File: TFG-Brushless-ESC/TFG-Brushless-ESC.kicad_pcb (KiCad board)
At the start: 4 copper layers, 100 x 51 mm, 140 parts, among them J1 MOTOR, J2 USB C Receptacle, J3 HALL SENSORS, J4 SWD-I2C, J5 24V IN, Q1 TK58E06N1, Q2 TK58E06N1, Q3 TK58E06N1, Q4 TK58E06N1, Q5 TK58E06N1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

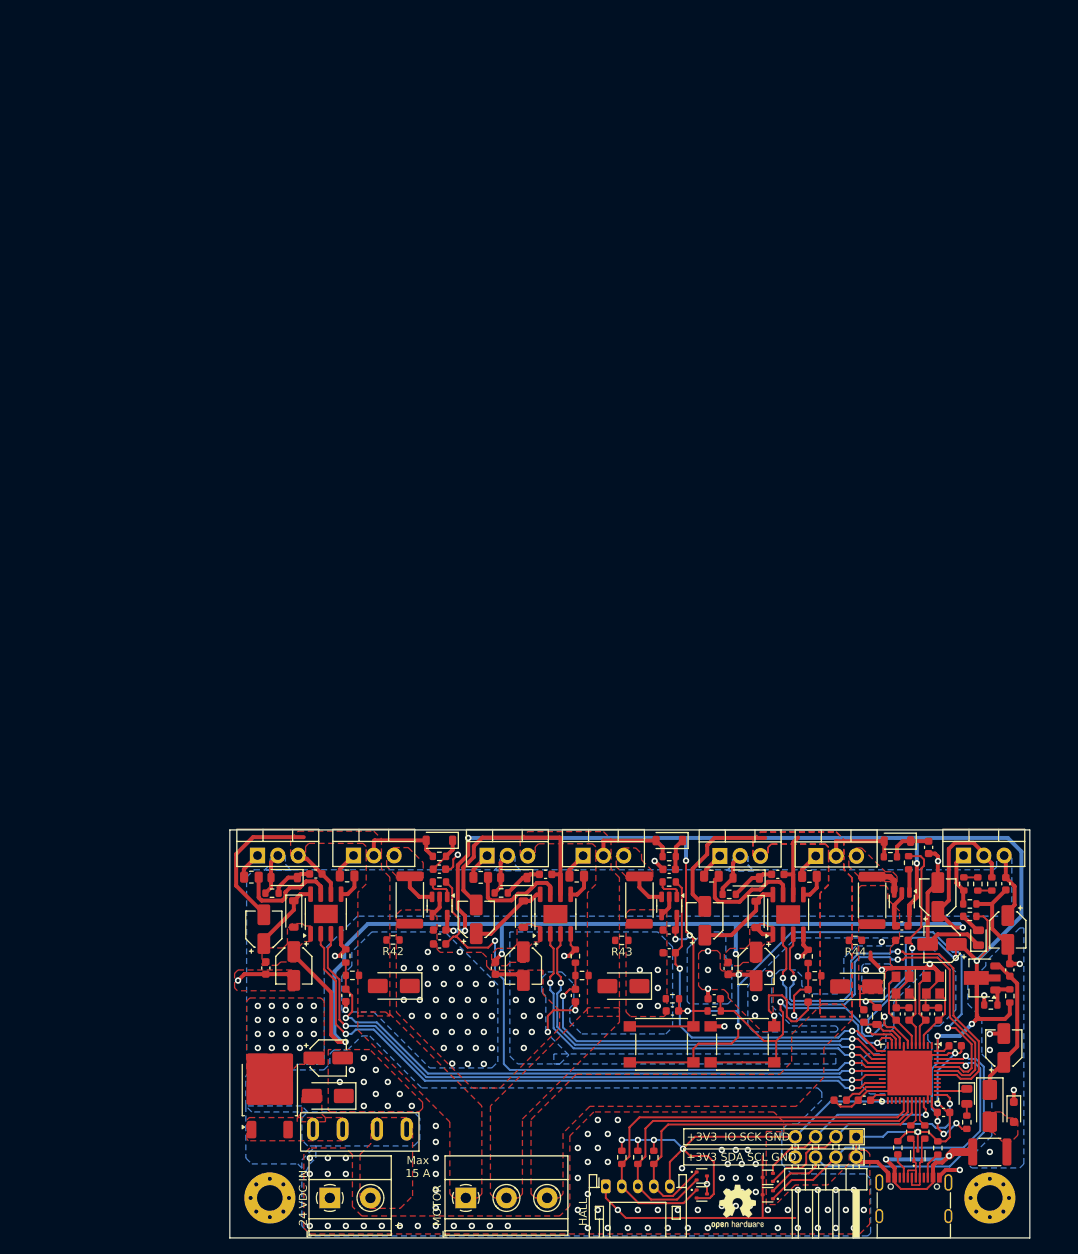
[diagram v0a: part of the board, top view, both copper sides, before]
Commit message: Change motor terminal blocks and new half bridge layaout
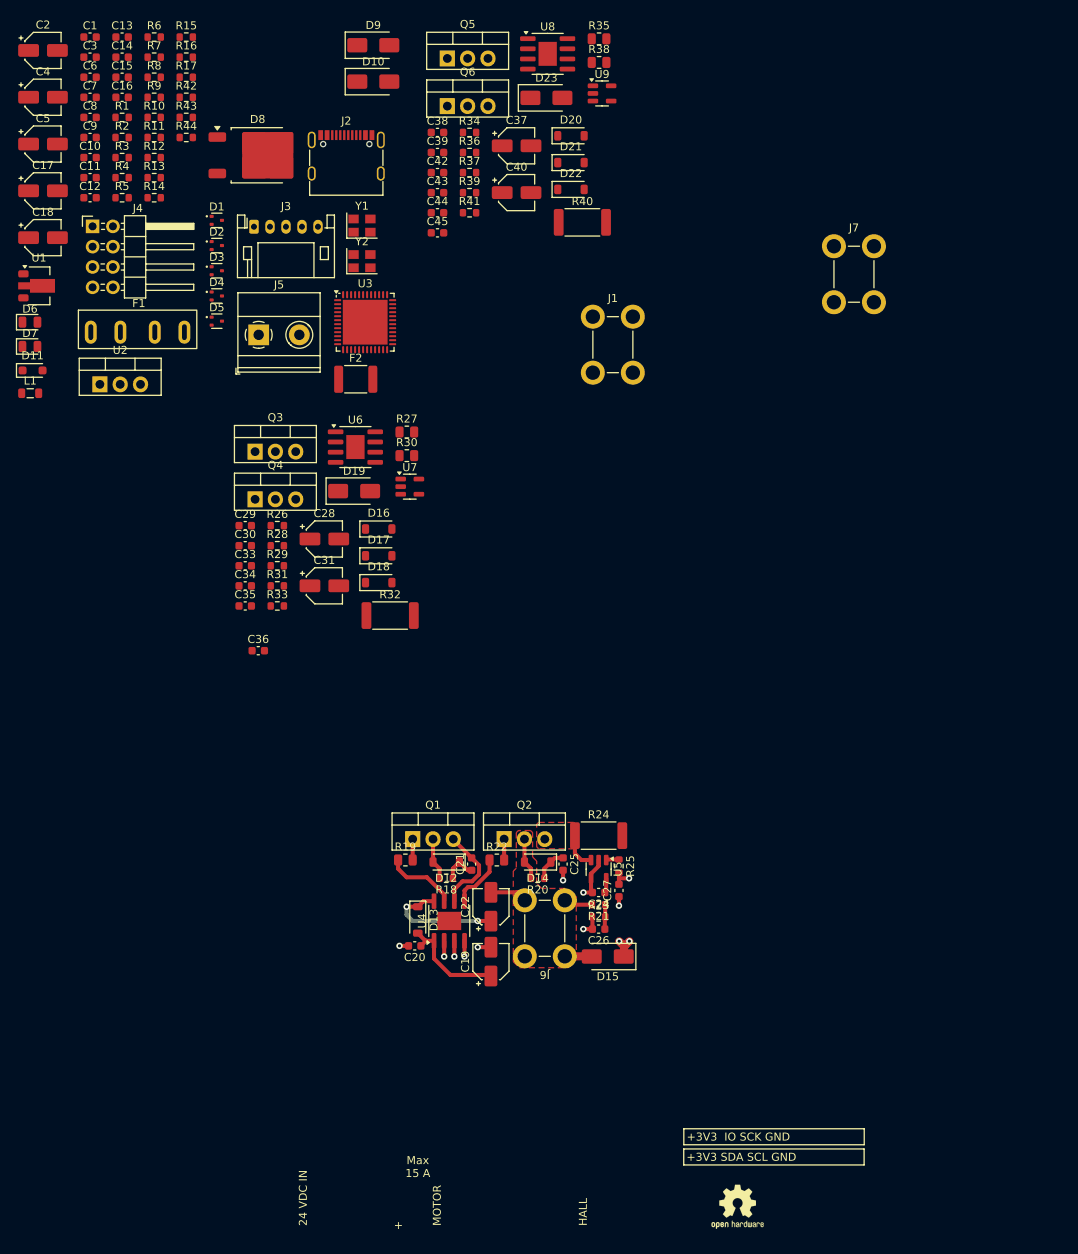
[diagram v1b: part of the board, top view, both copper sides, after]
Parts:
- removed the REF** at (139.3, 161.5)
- removed the REF** at (49.3, 161.5)
- removed the REF** at (116.8, 162.5)
- removed SW1: BOOT0, Button_Switch_SMD:SW_Push_1P1T_NO_6x6mm_H9.5mm
- removed SW2: NRST, Button_Switch_SMD:SW_Push_1P1T_NO_6x6mm_H9.5mm
- added J6: U, TFG-Brushless-ESC:Screw_Terminal, F.Cu at (83.6, 127.9)
- added J7: W, TFG-Brushless-ESC:Screw_Terminal, F.Cu at (122.3, 46.0)
- F1: value 15A -> 20A
- J1: value MOTOR -> V; footprint TerminalBlock_Phoenix:TerminalBlock_Phoenix_MKDS-1,5-3-5.08_1x03_P5.08mm_Horizontal -> TFG-Brushless-ESC:Screw_Terminal
- moved C7 165.8 mm to (26.8, 23.9)
- moved C1 163.8 mm to (26.8, 16.4), turned to 0 degrees
- moved R17 163.0 mm to (38.8, 21.4), turned to 0 degrees
- moved R10 161.8 mm to (34.8, 26.5), turned to 0 degrees
- moved R9 160.9 mm to (34.8, 23.9), turned to 0 degrees
- moved R6 159.9 mm to (34.8, 16.4), turned to 0 degrees
- moved C4 159.3 mm to (20.9, 23.9), turned to 0 degrees
- moved C2 158.5 mm to (20.9, 18.1), turned to 0 degrees
- moved C14 157.2 mm to (30.8, 18.9), turned to 0 degrees
- moved C18 157.1 mm to (20.9, 41.5), turned to 0 degrees
- moved C9 156.8 mm to (26.8, 29.0)
- moved C8 156.4 mm to (26.8, 26.5), turned to 0 degrees
- moved R11 156.2 mm to (34.8, 29.0), turned to 0 degrees
- moved R1 156.1 mm to (30.8, 26.5), turned to 0 degrees
- moved C13 155.8 mm to (30.8, 16.4), turned to 0 degrees
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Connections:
- J1 pad 1: /U -> /V
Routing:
- net +3V3: track 303.3 -> 1.86 mm, vias 20 -> 0
- net GND: track 242.3 -> 19.8 mm, vias 171 -> 9
- net +12V: track 142.0 -> 13.5 mm, vias 4 -> 0
- net /BOOT0: track 86.4 -> 0.00 mm, vias 3 -> 0
- net /PB10: track 84.4 -> 1.97 mm, vias 2 -> 1
- net /PB1: track 82.7 -> 1.97 mm, vias 2 -> 1
- net /PA7: track 79.2 -> 2.79 mm, vias 2 -> 1
- net /PB0: track 77.7 -> 3.07 mm, vias 2 -> 0
- net /PA6: track 55.2 -> 0.00 mm, vias 2 -> 0
- net /PA8: track 55.1 -> 0.00 mm
- net /PB6: track 54.9 -> 0.00 mm, vias 2 -> 0
- net /PA5: track 54.4 -> 0.00 mm, vias 2 -> 0
- net /PB7: track 54.1 -> 0.00 mm, vias 2 -> 0
- net /PA9: track 51.8 -> 0.00 mm
- net /PA4: track 50.7 -> 0.00 mm, vias 2 -> 0
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- removed copper zone on F.Cu, net +12V
- removed copper zone on B.Cu, net +24V
- removed copper zone on F.Cu, net +24V
- removed copper zone on F.Cu, net /24V fused
- removed copper zone on F.Cu, net /24V in
- removed copper zone on F.Cu, net /5V fused
- removed copper zone on F.Cu, net /Half-Bridge-V/Shunt
- removed copper zone on F.Cu, net /Half-Bridge-W/Shunt
- removed copper zone on F.Cu, net /V
- removed copper zone on F.Cu, net /W
- removed copper zone on B.Cu, net GND
- removed copper zone on F.Cu, net GND
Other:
- board outline removed
- board text removed: "Designed by humans on Earth"
- board text removed: "Dimensions: 100 x 51 mm Distance between screw holes: 90 mm"
- board text removed: "Mira a la pizarra"
- board text removed: "github.com/AdriTeixeHax"

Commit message: PCB v2
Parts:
- added D24: DESD5V0U1BA, Diode_SMD:D_SOD-323_HandSoldering, F.Cu at (108.6, 154.4)
- added D25: DESD5V0U1BA, Diode_SMD:D_SOD-323_HandSoldering, F.Cu at (72.5, 150.2)
- added R45: 10k, Resistor_SMD:R_0603_1608Metric, F.Cu at (150.7, 157.3)
- added R46: 10k, Resistor_SMD:R_0603_1608Metric, F.Cu at (150.7, 161.3)
- added REF**: MountingHole_3.2mm_M3_Pad_Via, MountingHole:MountingHole_3.2mm_M3_Pad_Via, F.Cu at (69.8, 141.1)
- added REF**: MountingHole_3.2mm_M3_Pad_Via, MountingHole:MountingHole_3.2mm_M3_Pad_Via, F.Cu at (154.9, 141.1)
- added SW1: BOOT0, Button_Switch_SMD:SW_Push_1P1T_NO_6x6mm_H9.5mm, F.Cu at (145.3, 142.1)
- added SW2: NRST, Button_Switch_SMD:SW_Push_1P1T_NO_6x6mm_H9.5mm, F.Cu at (135.0, 142.1)
- F1: value 20A -> 15A
- J2: footprint Connector_USB:USB_C_Receptacle_G-Switch_GT-USB-7010ASV -> Connector_USB:USB_C_Receptacle_XKB_U262-16XN-4BVC11
- moved C6 168.5 mm to (148.5, 138.0)
- moved C2 166.6 mm to (114.8, 155.7), turned to 180 degrees
- moved R6 165.6 mm to (125.0, 155.2), turned to 180 degrees
- moved C1 163.2 mm to (109.7, 157.0), turned to 180 degrees
- moved J4 162.8 mm to (147.1, 150.1), turned to -90 degrees
- moved R10 161.6 mm to (135.8, 152.6), turned to 180 degrees
- moved C14 160.0 mm to (124.7, 148.4)
- moved R9 159.0 mm to (128.2, 152.6)
- moved R1 158.3 mm to (125.0, 153.7)
- moved R2 158.2 mm to (145.5, 138.0), turned to 180 degrees
- moved D1 158.2 mm to (150.3, 155.2)
- moved C13 157.7 mm to (124.7, 143.1)
- moved C7 157.5 mm to (121.6, 149.8)
- moved C15 156.7 mm to (124.7, 146.9)
- moved R15 153.9 mm to (91.5, 161.1), turned to 180 degrees
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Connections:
- D3 pad 1: /PA10 -> /PA8
- D4 pad 1: /PA8 -> /PA10
- R13 pad 1: /PA10 -> /PA8
- R15 pad 1: /PA8 -> /PA10
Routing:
- net +3V3: track 1.86 -> 281.3 mm, vias 0 -> 10
- net GND: track 19.8 -> 206.2 mm, vias 9 -> 69
- net +12V: track 13.5 -> 134.4 mm
- net /BOOT0: track 0.00 -> 63.5 mm, vias 0 -> 2
- net /PA7: track 2.79 -> 62.6 mm, vias 1 -> 2
- net /PA0: track 0.00 -> 59.6 mm, vias 0 -> 2
- net /PB1: track 1.97 -> 59.9 mm, vias 1 -> 2
- net +24V: track 5.24 -> 62.9 mm, vias 0 -> 16
- net /PB10: track 1.97 -> 59.0 mm, vias 1 -> 2
- net /SWDIO: track 0.00 -> 55.8 mm, vias 0 -> 1
- net /PB0: track 3.07 -> 58.2 mm, vias 0 -> 2
- net /PA1: track 0.00 -> 54.5 mm, vias 0 -> 2
- net /SWSCK: track 0.00 -> 48.3 mm, vias 0 -> 1
- net /I2C_SDA: track 0.00 -> 46.4 mm
- net /USB_R_N: track 0.00 -> 46.1 mm, vias 0 -> 2
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- added copper zone on F.Cu, net +12V
- added copper zone on B.Cu, net +24V
- added copper zone on F.Cu, net +24V
- added copper zone on F.Cu, net /24V fused
- added copper zone on F.Cu, net /24V in
- added copper zone on F.Cu, net /Half-Bridge-V/Shunt
- added copper zone on F.Cu, net /Half-Bridge-W/Shunt
- added copper zone on F.Cu, net /V
- added copper zone on F.Cu, net /W
- added copper zone on F.Cu, net GND
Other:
- board outline added: 95.4 x 49.3 mm
- board text added: "3V3 IO SCK GND"
- board text added: "3V3 SDA SCL GND"
- board text removed: "+3V3 IO SCK GND"
- board text removed: "+3V3 SDA SCL GND"

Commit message: PCB v3
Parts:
- removed the REF** at (69.8, 141.1)
- removed the REF** at (154.9, 141.1)
- added ?: , , F.Cu at (104.3, 59.3)
- added REF**: MountingHole_2.2mm_M2_Pad_Via, MountingHole:MountingHole_2.2mm_M2_Pad_Via, F.Cu at (104.3, 94.7)
- added REF**: MountingHole_2.2mm_M2_Pad_Via, MountingHole:MountingHole_2.2mm_M2_Pad_Via, F.Cu at (204.3, 57.7)
- added REF**: MountingHole_2.2mm_M2_Pad_Via, MountingHole:MountingHole_2.2mm_M2_Pad_Via, F.Cu at (104.3, 57.7)
- added REF**: MountingHole_2.2mm_M2_Pad_Via, MountingHole:MountingHole_2.2mm_M2_Pad_Via, F.Cu at (204.3, 94.7)
- D8: value FERD30H100SB -> STPS30100ST; footprint Package_TO_SOT_SMD:TO-252-2 -> Package_TO_SOT_THT:TO-220-3_Vertical
- moved SW1 94.3 mm to (203.7, 68.0), turned to -90 degrees
- moved SW2 93.7 mm to (203.7, 78.3), turned to -90 degrees
- moved R13 93.7 mm to (156.4, 90.5), turned to -90 degrees
- moved R14 92.6 mm to (156.4, 93.5), turned to -90 degrees
- moved R15 91.5 mm to (156.4, 96.6), turned to -90 degrees
- moved R46 91.2 mm to (203.5, 86.9)
- moved D3 90.9 mm to (162.8, 88.7)
- moved D4 90.9 mm to (166.8, 88.7)
- moved J3 90.9 mm to (159.8, 91.9)
- moved REF** 89.4 mm to (119.0, 77.0)
- moved C6 89.3 mm to (199.6, 64.8), turned to 90 degrees
- moved C8 89.1 mm to (182.2, 93.5)
- moved R2 88.6 mm to (199.6, 67.8), turned to -90 degrees
- moved D7 88.5 mm to (175.8, 94.4)
- moved R17 88.5 mm to (172.5, 94.4)
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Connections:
- net Net-(D13-K) renamed /Half-Bridge-U/VB
- net Net-(D17-K) renamed /Half-Bridge-V/VB
- net Net-(D21-K) renamed /Half-Bridge-W/VB
- C26 pad 1: /PB0 -> /PB1
- C27 pad 2: /PA7 -> /PB0
- C35 pad 1: /PA4 -> /PA5
- C36 pad 2: /PA3 -> /PA4
- D3 pad 1: /PA8 -> /PB3
- D3 pad 2: /PA9 -> /PB4
- D4 pad 1: /PA10 -> /PB5
- J3 pad 2: /PA8 -> /PB3
- J3 pad 3: /PA9 -> /PB4
- J3 pad 4: /PA10 -> /PB5
- J5 pad 1: GND -> /24V in
- J5 pad 2: /24V in -> GND
- R13 pad 1: /PA8 -> /PB3
- R14 pad 1: /PA9 -> /PB4
- R15 pad 1: /PA10 -> /PB5
- R21 pad 1: /PB0 -> /PB1
- R23 pad 2: /PB0 -> /PB1
- R25 pad 2: /PA7 -> /PB0
- R29 pad 1: /PA4 -> /PA5
- R31 pad 2: /PA4 -> /PA5
- R33 pad 2: /PA3 -> /PA4
- U4 pad 2: /PB10 -> /PA9
- U4 pad 3: /PB1 -> /PA8
- U6 pad 2: /PA6 -> /PA7
- U6 pad 3: /PA5 -> /PA6
- U8 pad 2: /PB7 -> /PA3
- U8 pad 3: /PB6 -> /PA2
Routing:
- net /PB10: track 59.0 -> 0.00 mm, vias 2 -> 0
- net /PB5: track 0.00 -> 44.1 mm
- net /PB4: track 0.00 -> 43.5 mm
- net /PB3: track 0.00 -> 42.8 mm
- net /PA10: track 37.2 -> 0.00 mm
- net /PB6: track 37.0 -> 0.00 mm, vias 2 -> 0
- net /PB7: track 34.7 -> 0.00 mm, vias 2 -> 0
- net /PA8: track 33.9 -> 65.0 mm
- net /PA9: track 35.4 -> 65.8 mm
- net /USB_R_N: track 46.1 -> 15.9 mm, vias 2 -> 0
- net /USB_R_P: track 45.5 -> 16.0 mm, vias 2 -> 0
- net /PA1: track 54.5 -> 30.1 mm, vias 2 -> 0
- net /PA7: track 62.6 -> 39.8 mm, vias 2 -> 0
- net /PA0: track 59.6 -> 38.7 mm, vias 2 -> 0
- net /SWSCK: track 48.3 -> 32.4 mm, vias 1 -> 2
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- added copper zone on In1.Cu, net /24V fused
- added copper zone on In2.Cu, net /24V fused
- added copper zone on B.Cu, net /24V in
- added copper zone on In1.Cu, net /24V in
- added copper zone on In2.Cu, net /24V in
- added copper zone on B.Cu, net /U
- added copper zone on In1.Cu, net /U
- added copper zone on In2.Cu, net /U
- added copper zone on B.Cu, net /V
- added copper zone on In1.Cu, net /V
- added copper zone on In2.Cu, net /V
- added copper zone on B.Cu, net /W
- added copper zone on In1.Cu, net /W
- added copper zone on In2.Cu, net /W
- added copper zone on B.Cu, net GND
- removed copper zone on F.Cu, net +12V
- removed copper zone on F.Cu, net +24V
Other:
- board size 95.4 x 49.3 mm -> 107 x 44 mm
- board text added: "24Vcc IN"
- board text added: "By AdriTeixeHax"
- board text added: "Hall"
- board text added: "RTSpeed"
- board text added: "USB Type C"
- board text added: "V IO CLK G V SCK SCL G"
- board text added: "_____________"
- board text added: "github.com/AdriTeixeHax"
- board text removed: "+"
- board text removed: "24 VDC IN"
- board text removed: "24V In"
- board text removed: "3V3 IO SCK GND"
- board text removed: "3V3 SDA SCL GND"
- board text removed: "HALL"
- board text removed: "MOTOR"
- board text removed: "Max 15 A"
- board text removed: "OUT"
- board text removed: "Reg 12V"
- board text removed: "Reg 5V"
- board text removed: "U"
- board text removed: "USB C"
- board text removed: "V"
- board text removed: "W"
- board text removed: "uC"

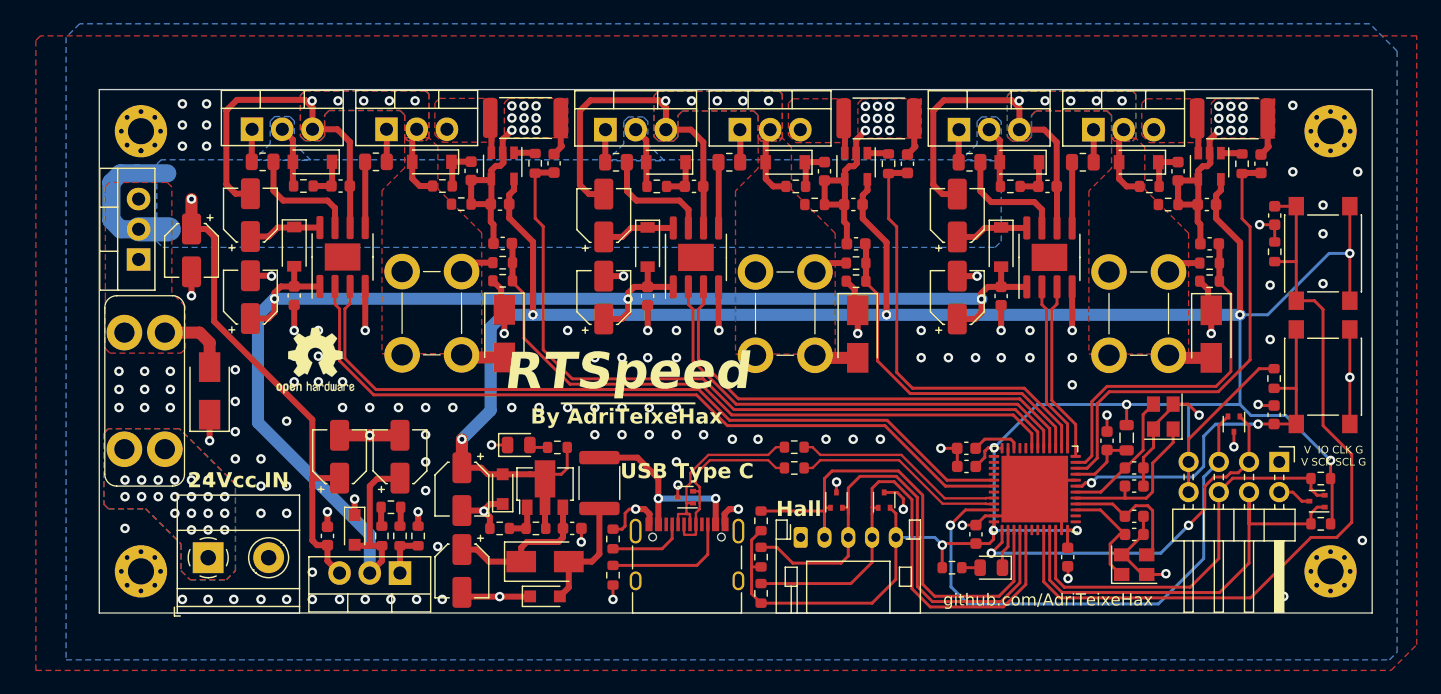
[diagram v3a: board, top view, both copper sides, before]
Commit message: updated main power connector to phoenix
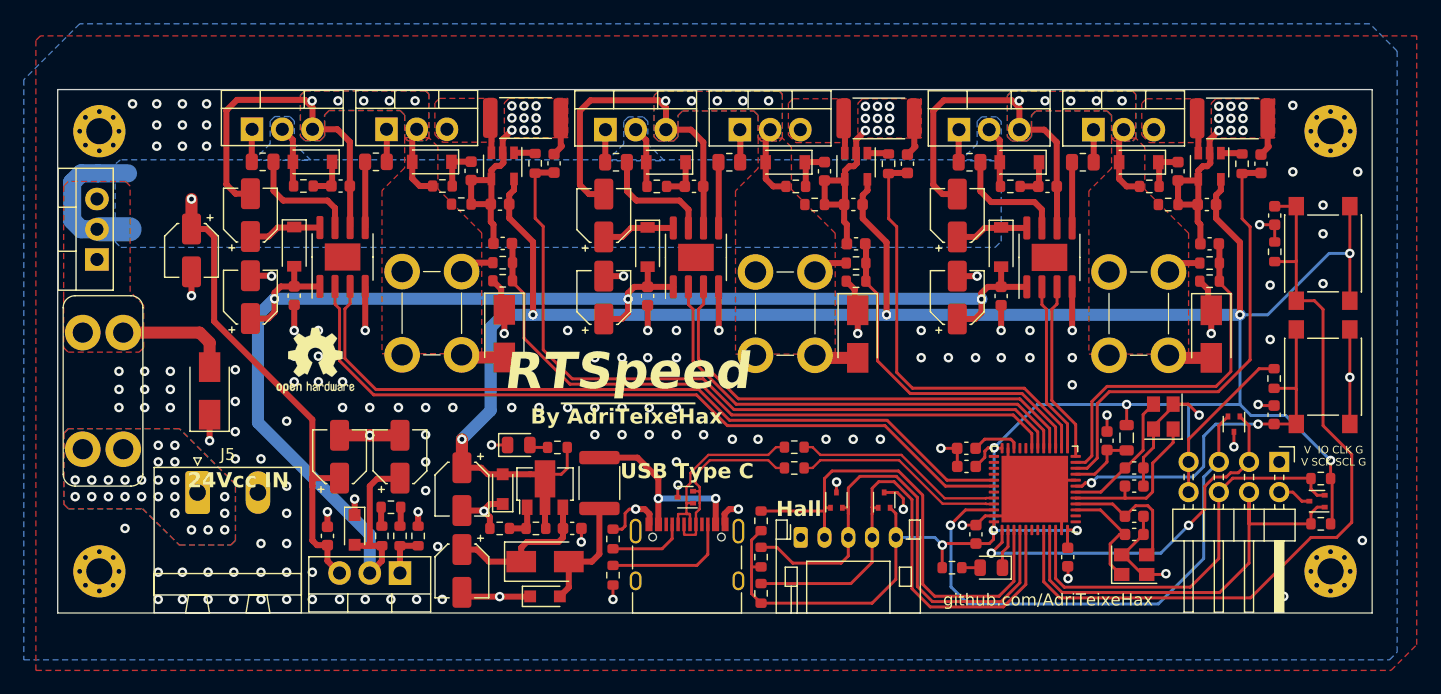
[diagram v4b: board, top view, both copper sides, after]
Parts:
- removed ?: , 
- J5: footprint TerminalBlock_Phoenix:TerminalBlock_Phoenix_MKDS-1,5-2-5.08_1x02_P5.08mm_Horizontal -> Connector_Phoenix_MSTB:PhoenixContact_MSTBA_2,5_2-G-5,08_1x02_P5.08mm_Horizontal
- moved J5 5.55 mm to (109.0, 88.1)
- moved D8 3.50 mm to (100.6, 68.5)
- moved F1 3.50 mm to (101.1, 79.5)
- moved REF** 3.50 mm to (100.8, 94.7)
- moved REF** 3.50 mm to (100.8, 57.7)
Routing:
- net /24V fused: track 6.17 -> 9.67 mm
- net GND: vias 161 -> 172
- net /24V in: vias 20 -> 24
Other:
- board size 107 x 44 mm -> 110.5 x 44 mm
